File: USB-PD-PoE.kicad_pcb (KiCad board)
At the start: 4 copper layers, 39.6 x 87.4 mm, 126 parts, among them J1 8P8C_Shielded, J2 8P8C_Shielded, J3 TagConnect_TC2030_SWD, J4 USB_C_Receptacle_USB2.0, Q1 FDC2512, Q2 2N7002, Q3 2N7002, Q4 2N7002, Q5 APM4953KC, T1 HR051142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

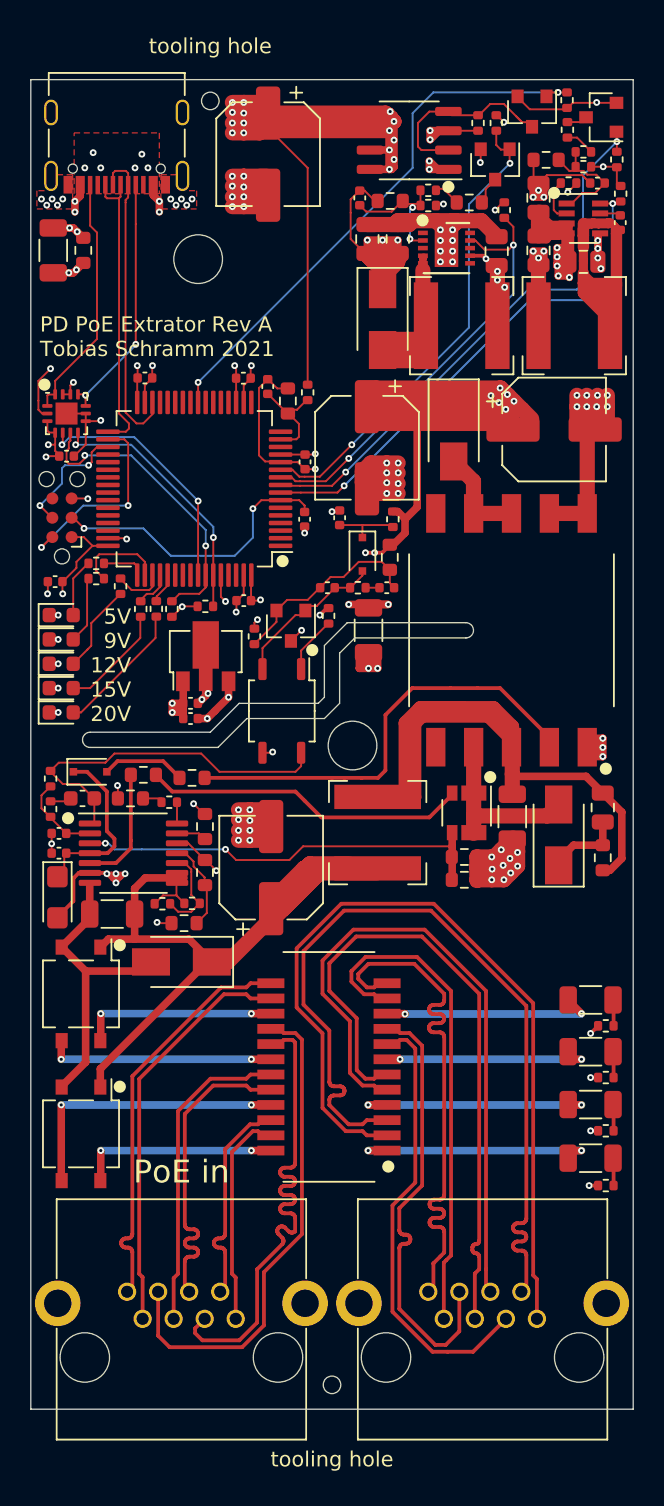
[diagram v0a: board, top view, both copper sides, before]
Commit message: Add tooling holes
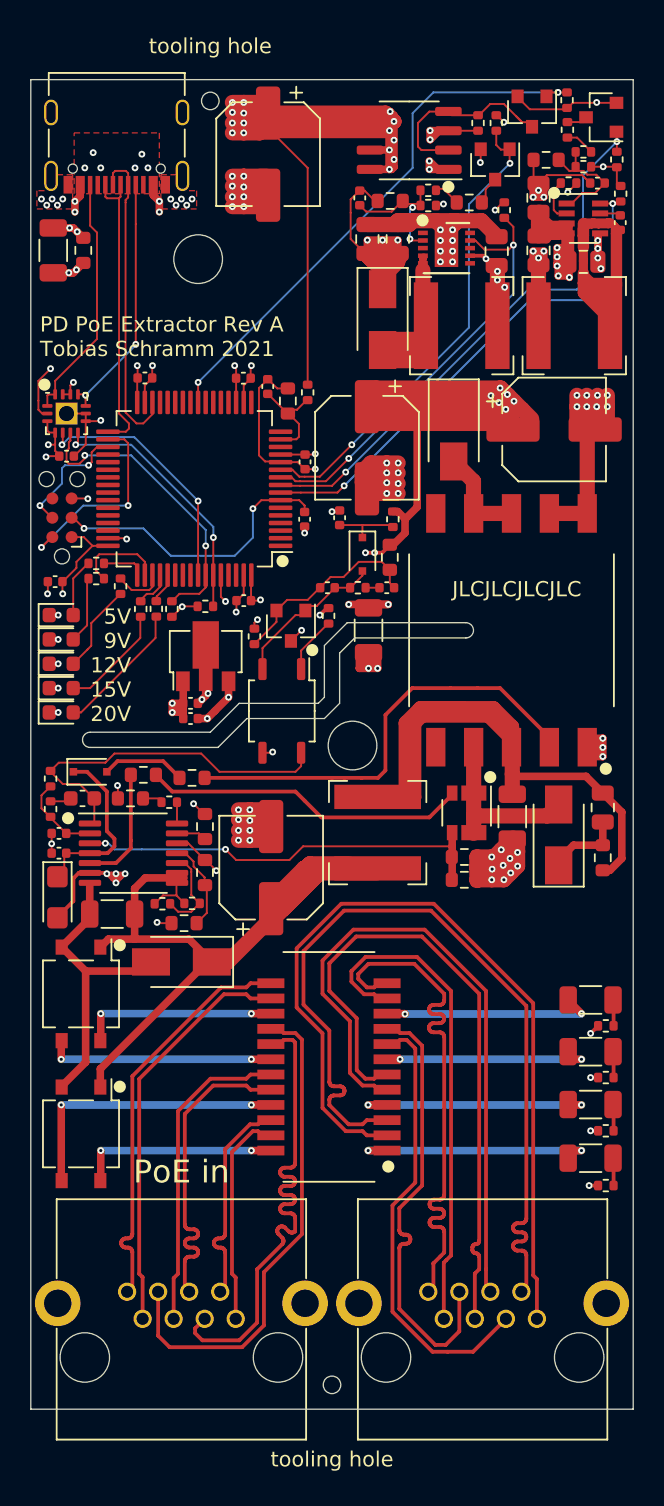
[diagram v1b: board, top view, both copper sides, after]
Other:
- board text added: "JLCJLCJLCJLC"
- board text added: "PD PoE Extractor Rev A Tobias Schramm 2021"
- board text removed: "PD PoE Extrator Rev A Tobias Schramm 2021"

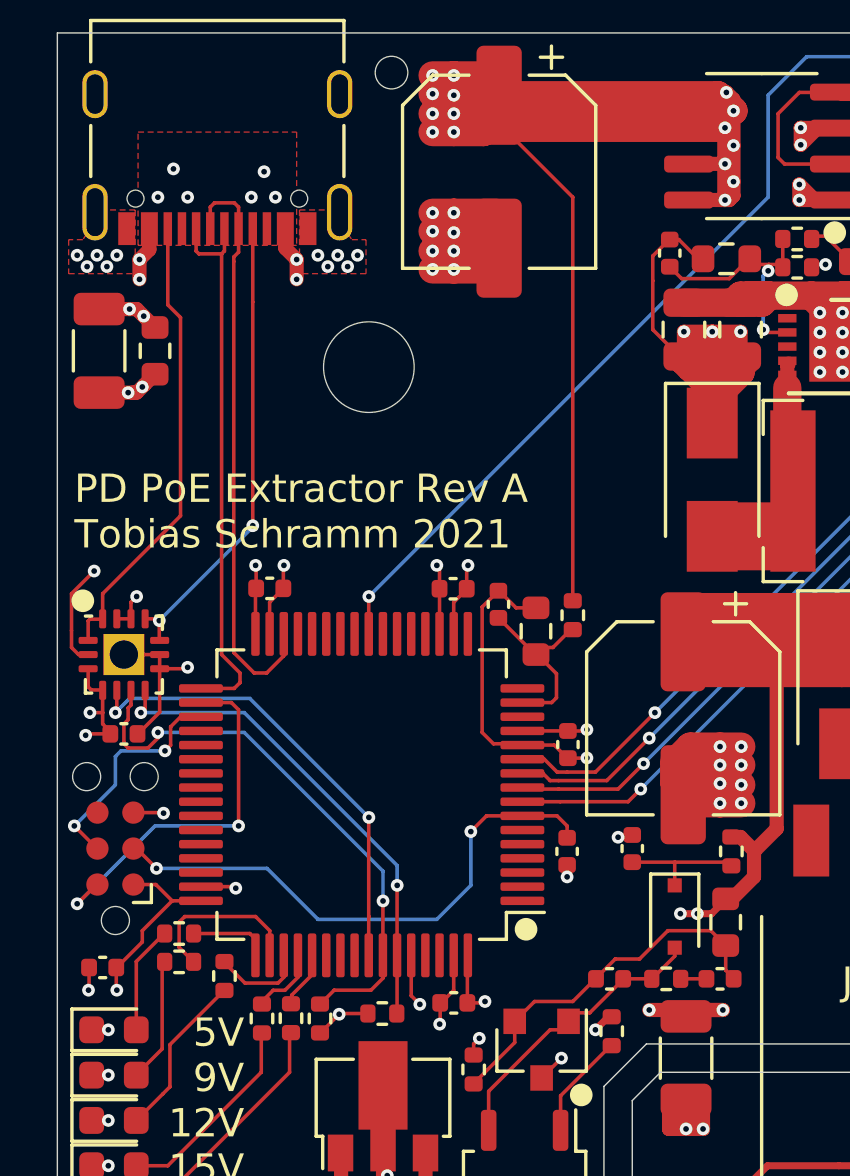
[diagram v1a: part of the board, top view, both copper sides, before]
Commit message: Fix PA <-> PB mixup
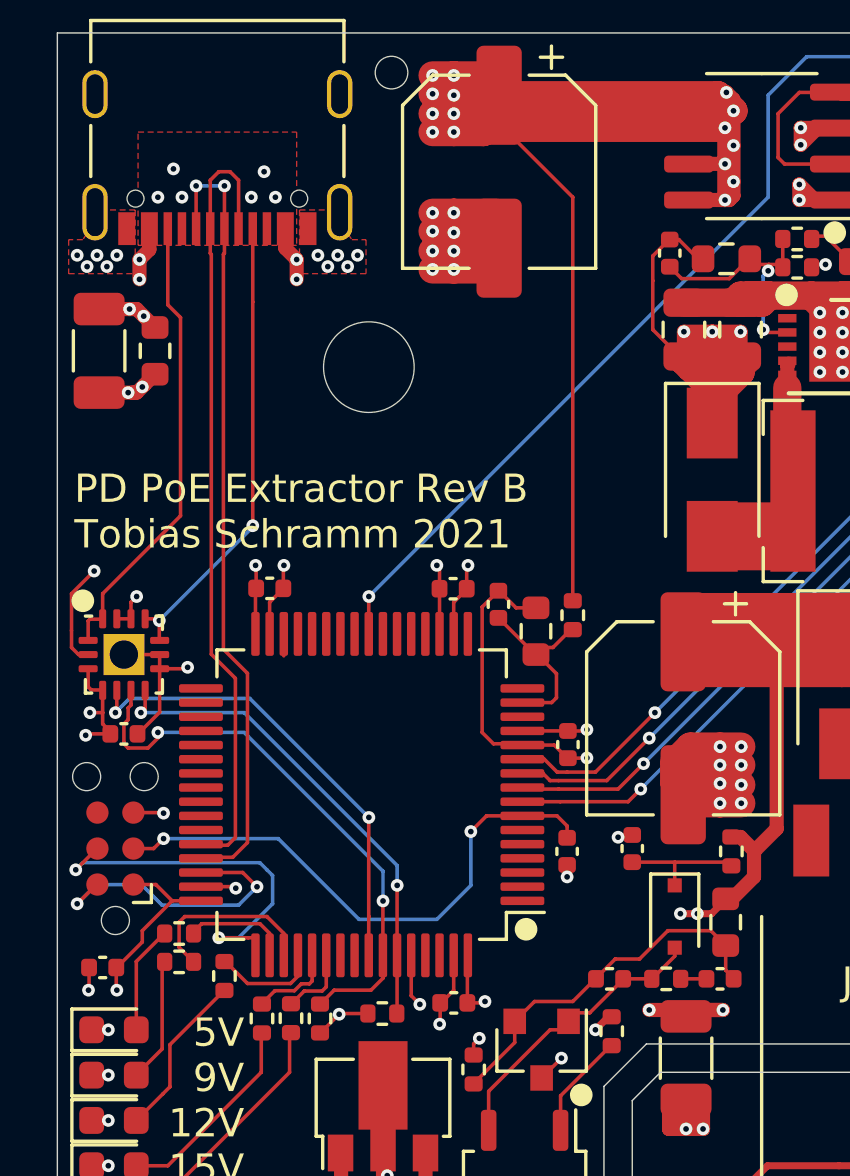
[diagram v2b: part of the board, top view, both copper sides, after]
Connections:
- U1 pad 30: /D- -> Net-(U1-Pad30)
- U1 pad 33: /D+ -> Net-(U1-Pad33)
- U1 pad 34: /SWDIO -> Net-(U1-Pad34)
- U1 pad 35: /SWCLK -> Net-(U1-Pad35)
- U1 pad 44: Net-(U1-Pad44) -> /D-
- U1 pad 45: Net-(U1-Pad45) -> /D+
- U1 pad 46: Net-(U1-Pad46) -> /SWDIO
- U1 pad 49: /LED_5V -> /SWCLK
- U1 pad 50: /LED_9V -> /LED_5V
- U1 pad 51: /LED_12V -> /LED_9V
- U1 pad 52: /LED_15V -> /LED_12V
- U1 pad 53: /LED_20V -> /LED_15V
- U1 pad 54: Net-(U1-Pad54) -> /LED_20V
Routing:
- net /D+: track 19.5 -> 27.9 mm, vias 0 -> 2
- net /D-: track 20.8 -> 27.9 mm
- net /SWCLK: track 8.18 -> 14.0 mm
- net /SWDIO: track 13.4 -> 10.4 mm
- net /LED_5V: track 2.77 -> 3.73 mm
- net Net-(U1-Pad30): track 0.00 -> 0.78 mm
- net /LED_20V: track 2.00 -> 2.61 mm
- net /LED_15V: track 2.47 -> 3.04 mm
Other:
- board text added: "PD PoE Extractor Rev B Tobias Schramm 2021"
- board text removed: "PD PoE Extractor Rev A Tobias Schramm 2021"
